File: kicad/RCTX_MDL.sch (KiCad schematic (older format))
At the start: 40 parts, among them P22 SW, P23 PWR_BUS, P24 TX_VCC, P25 MULTI_DIGITAL_1, P26 PWR_BUS, P27 LEDS, P28 PWR_BUS, P29 MULTI_DIGITAL_2, P30 PWR_BUS, SW1 LEFT_3P1V, SW1 Reset, SW10 RIGHT_3P1V, SW11 RIGHT_3P1V, SW12 RIGHT_3P1V, SW13 RIGHT_3P1V, SW14 RIGHT_3P1V, SW15 RIGHT_3P1V, SW16 RIGHT_3P1V, SW17 RF_SWITCH_3P2V, SW18 LEFT_3P2V, SW19 RIGHT_3P2V_B, SW2 LEFT_3P1V, SW2 Program, SW20 RIGHT_3P2V_A, SW3 LEFT_3P1V, SW3 User, SW4 LEFT_3P1V, SW5 LEFT_3P1V, SW6 LEFT_3P1V, SW7 LEFT_3P1V, SW8 LEFT_3P1V, SW9 RIGHT_3P1V

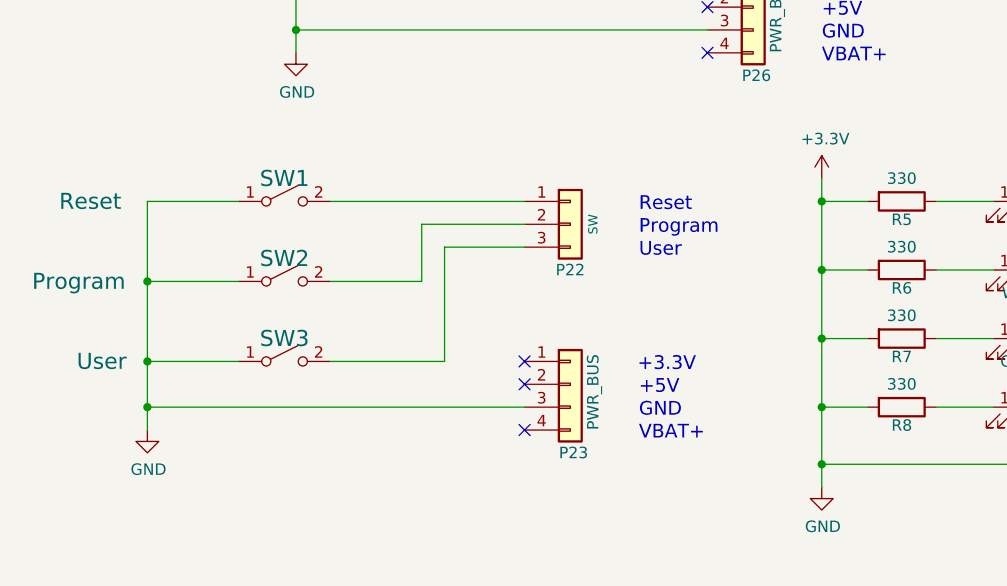
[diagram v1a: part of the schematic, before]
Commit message: Using ERF32FG12 SoC instead of PIC32MX
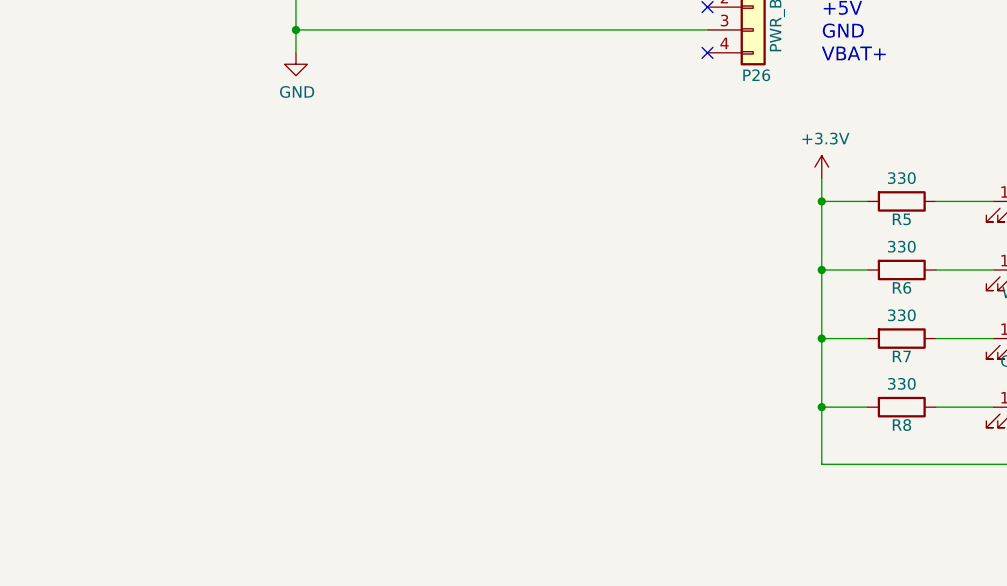
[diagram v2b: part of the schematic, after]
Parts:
- removed P22: SW, Connectors_Samtec:SL-103-X-XX_1x03, symbol RCTX-rescue:Conn_01x03-conn
- removed P23: PWR_BUS, Connectors_Samtec:SL-104-X-XX_1x04, symbol RCTX-rescue:Conn_01x04-conn
- removed SW1: Reset, Buttons_Switches_THT:SW_PUSH_6mm_h5mm, symbol RCTX-rescue:SW_SPST-switches
- removed SW2: Program, Buttons_Switches_THT:SW_PUSH_6mm_h5mm, symbol RCTX-rescue:SW_SPST-switches
- removed SW3: User, Buttons_Switches_THT:SW_PUSH_6mm_h5mm, symbol RCTX-rescue:SW_SPST-switches
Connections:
- net +3V3: no longer P26.3 (Pin_3), P30.3 (Pin_3), SW1.3, SW10.3, SW11.3, SW12.3, SW13.3, SW14.3, SW15.3, SW16.3, SW18.4, SW2.3, SW20.4, SW3.3, SW4.3, SW5.3, SW6.3, SW7.3, SW8.3, SW9.3
- new net GND: P26.3 (Pin_3), P30.3 (Pin_3), SW1.3, SW10.3, SW11.3, SW12.3, SW13.3, SW14.3, SW15.3, SW16.3, SW18.4, SW2.3, SW20.4, SW3.3, SW4.3, SW5.3, SW6.3, SW7.3, SW8.3, SW9.3
- no-connect marks 18 -> 15
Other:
- note removed: "Program"
- note removed: "Reset"
- note removed: "User"
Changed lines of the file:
@@
 $Descr A4 11693 8268
 encoding utf-8
-Sheet 8 11
+Sheet 8 13
 Title "LEDs and Switches (User, RF mode, Multi digital)"
 Date "2020-04-15"
@@
 Wire Wire Line
 	1900 4550 2400 4550
-Wire Wire Line
-	1250 6450 1250 6100
-Wire Wire Line
-	1250 6100 1250 5750
-$Comp
-L RCTX-rescue:SW_SPST-switches SW1
-U 1 1 4EB6D083
-P 1850 5750
-F 0 "SW1" H 1850 5850 70  0000 C CNN
-F 1 "Reset" H 1000 5750 70  0000 C CNN
-F 2 "Buttons_Switches_THT:SW_PUSH_6mm_h5mm" H 1850 5750 50  0001 C CNN
-F 3 "" H 1850 5750 50  0001 C CNN
-	1    1850 5750
-	1    0    0    -1
-$EndComp
-$Comp
-L RCTX-rescue:SW_SPST-switches SW2
-U 1 1 4EB6D08C
-P 1850 6100
-F 0 "SW2" H 1850 6200 70  0000 C CNN
-F 1 "Program" H 950 6100 70  0000 C CNN
-F 2 "Buttons_Switches_THT:SW_PUSH_6mm_h5mm" H 1850 6100 50  0001 C CNN
-F 3 "" H 1850 6100 50  0001 C CNN
-	1    1850 6100
-	1    0    0    -1
-$EndComp
-$Comp
-L RCTX-rescue:SW_SPST-switches SW3
-U 1 1 4EB6D091
-P 1850 6450
-F 0 "SW3" H 1850 6550 70  0000 C CNN
-F 1 "User" H 1050 6450 70  0000 C CNN
-F 2 "Buttons_Switches_THT:SW_PUSH_6mm_h5mm" H 1850 6450 50  0001 C CNN
-F 3 "" H 1850 6450 50  0001 C CNN
-	1    1850 6450
-	1    0    0    -1
-$EndComp
-$Comp
-L RCTX-rescue:Conn_01x03-conn P22
-U 1 1 4EB6D0B4
-P 3100 5850
-F 0 "P22" H 3100 5650 50  0000 C CNN
-F 1 "SW" V 3200 5850 40  0000 C CNN
-F 2 "Connectors_Samtec:SL-103-X-XX_1x03" H 3100 5850 50  0001 C CNN
-F 3 "" H 3100 5850 50  0001 C CNN
-	1    3100 5850
-	1    0    0    -1
-$EndComp
-NoConn ~ 2900 6450
-NoConn ~ 2900 6550
-NoConn ~ 2900 6750
-Text Notes 3400 5800 0    60   ~ 0
-Reset
-Text Notes 3400 5900 0    60   ~ 0
-Program
-Text Notes 3400 6000 0    60   ~ 0
-User
-Connection ~ 1250 6450
-Wire Wire Line
-	1250 6450 1650 6450
-Wire Wire Line
-	1250 5750 1650 5750
-Wire Wire Line
-	1250 6650 1250 6450
-Wire Wire Line
-	2900 6650 1250 6650
-Wire Wire Line
-	2450 5850 2900 5850
-Wire Wire Line
-	2450 6100 2450 5850
-Wire Wire Line
-	2050 6100 2450 6100
-Wire Wire Line
-	2900 5750 2050 5750
-Wire Wire Line
-	2550 6450 2050 6450
-Wire Wire Line
-	2550 5950 2550 6450
-Wire Wire Line
-	2900 5950 2550 5950
-Wire Wire Line
-	1250 6100 1650 6100
-Connection ~ 1250 6100
 $Comp
 L RCTX-rescue:Conn_01x02-conn P?
@@
 	1    0    0    -1
 $EndComp
-Text Notes 3650 6500 2    60   ~ 0
-+3.3V
-Text Notes 3400 6700 0    60   ~ 0
-GND
-Text Notes 3400 6600 0    60   ~ 0
-+5V
-Text Notes 3400 6800 0    60   ~ 0
-VBAT+
-$Comp
-L RCTX-rescue:Conn_01x04-conn P23
-U 1 1 5DEA4D3C
-P 3100 6550
-F 0 "P23" H 3050 6250 50  0000 L CNN
-F 1 "PWR_BUS" V 3200 6350 50  0000 L CNN
-F 2 "Connectors_Samtec:SL-104-X-XX_1x04" H 3100 6550 50  0001 C CNN
-F 3 "~" H 3100 6550 50  0001 C CNN
-	1    3100 6550
-	1    0    0    -1
-$EndComp
 Text Notes 6550 6950 2    60   ~ 0
 +3.3V
@@
 $EndComp
 $Comp
+L RCTX-rescue:+3.3V-power #PWR013
+U 1 1 5F86063A
+P 2000 1100
+F 0 "#PWR013" H 2000 950 50  0001 C CNN
+F 1 "+3.3V" H 2015 1273 50  0000 C CNN
+F 2 "" H 2000 1100 50  0001 C CNN
+F 3 "" H 2000 1100 50  0001 C CNN
+	1    2000 1100
+	1    0    0    -1
+$EndComp
+$Comp
+L RCTX-rescue:GND-power #PWR016
+U 1 1 5F861623
+P 7150 5150
+F 0 "#PWR016" H 7150 4900 50  0001 C CNN
+F 1 "GND" H 7155 4977 50  0000 C CNN
+F 2 "" H 7150 5150 50  0001 C CNN
+F 3 "" H 7150 5150 50  0001 C CNN
+	1    7150 5150
+	1    0    0    -1
+$EndComp
+$Comp
+L RCTX-rescue:GND-power #PWR012
+U 1 1 5F864106
+P 1900 5100
+F 0 "#PWR012" H 1900 4850 50  0001 C CNN
+F 1 "GND" H 1905 4927 50  0000 C CNN
+F 2 "" H 1900 5100 50  0001 C CNN
+F 3 "" H 1900 5100 50  0001 C CNN
+	1    1900 5100
+	1    0    0    -1
+$EndComp
+Wire Wire Line
+	7250 1100 7250 1200
+Connection ~ 7250 1200
+Wire Wire Line
+	7150 5050 7150 5150
+Connection ~ 7150 5050
+Wire Wire Line
+	1900 5000 1900 5100
+Connection ~ 1900 5000
+Wire Wire Line
+	2000 1100 2000 1150
+Connection ~ 2000 1150
+Wire Wire Line
+	4200 5650 4200 5750
+Connection ~ 4200 5750
+$Comp
 L RCTX-rescue:+3.3V-power #PWR014
 U 1 1 5F85F799
@@
 	1    0    0    -1
 $EndComp
-$Comp
-L RCTX-rescue:+3.3V-power #PWR013
-U 1 1 5F86063A
-P 2000 1100
-F 0 "#PWR013" H 2000 950 50  0001 C CNN
-F 1 "+3.3V" H 2015 1273 50  0000 C CNN
-F 2 "" H 2000 1100 50  0001 C CNN
-F 3 "" H 2000 1100 50  0001 C CNN
-	1    2000 1100
-	1    0    0    -1
-$EndComp
-$Comp
-L RCTX-rescue:GND-power #PWR016
-U 1 1 5F861623
-P 7150 5150
-F 0 "#PWR016" H 7150 4900 50  0001 C CNN
-F 1 "GND" H 7155 4977 50  0000 C CNN
-F 2 "" H 7150 5150 50  0001 C CNN
-F 3 "" H 7150 5150 50  0001 C CNN
-	1    7150 5150
-	1    0    0    -1
-$EndComp
-$Comp
-L RCTX-rescue:GND-power #PWR015
-U 1 1 5F862221
-P 4200 7000
-F 0 "#PWR015" H 4200 6750 50  0001 C CNN
-F 1 "GND" H 4205 6827 50  0000 C CNN
-F 2 "" H 4200 7000 50  0001 C CNN
-F 3 "" H 4200 7000 50  0001 C CNN
-	1    4200 7000
-	1    0    0    -1
-$EndComp
-$Comp
-L RCTX-rescue:GND-power #PWR011
-U 1 1 5F863347
-P 1250 6750
-F 0 "#PWR011" H 1250 6500 50  0001 C CNN
-F 1 "GND" H 1255 6577 50  0000 C CNN
-F 2 "" H 1250 6750 50  0001 C CNN
-F 3 "" H 1250 6750 50  0001 C CNN
-	1    1250 6750
-	1    0    0    -1
-$EndComp
-$Comp
-L RCTX-rescue:GND-power #PWR012
-U 1 1 5F864106
-P 1900 5100
-F 0 "#PWR012" H 1900 4850 50  0001 C CNN
-F 1 "GND" H 1905 4927 50  0000 C CNN
-F 2 "" H 1900 5100 50  0001 C CNN
-F 3 "" H 1900 5100 50  0001 C CNN
-	1    1900 5100
-	1    0    0    -1
-$EndComp
-Wire Wire Line
-	7250 1100 7250 1200
-Connection ~ 7250 1200
-Wire Wire Line
-	7150 5050 7150 5150
-Connection ~ 7150 5050
-Wire Wire Line
-	4200 6900 4200 7000
-Connection ~ 4200 6900
-Wire Wire Line
-	1250 6650 1250 6750
-Connection ~ 1250 6650
-Wire Wire Line
-	1900 5000 1900 5100
-Connection ~ 1900 5000
-Wire Wire Line
-	2000 1100 2000 1150
-Connection ~ 2000 1150
-Wire Wire Line
-	4200 5650 4200 5750
-Connection ~ 4200 5750
 $EndSCHEMATC
